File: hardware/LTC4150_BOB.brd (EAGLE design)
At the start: 15.2 x 30.5 mm, 23 parts, among them U1 LTC4150

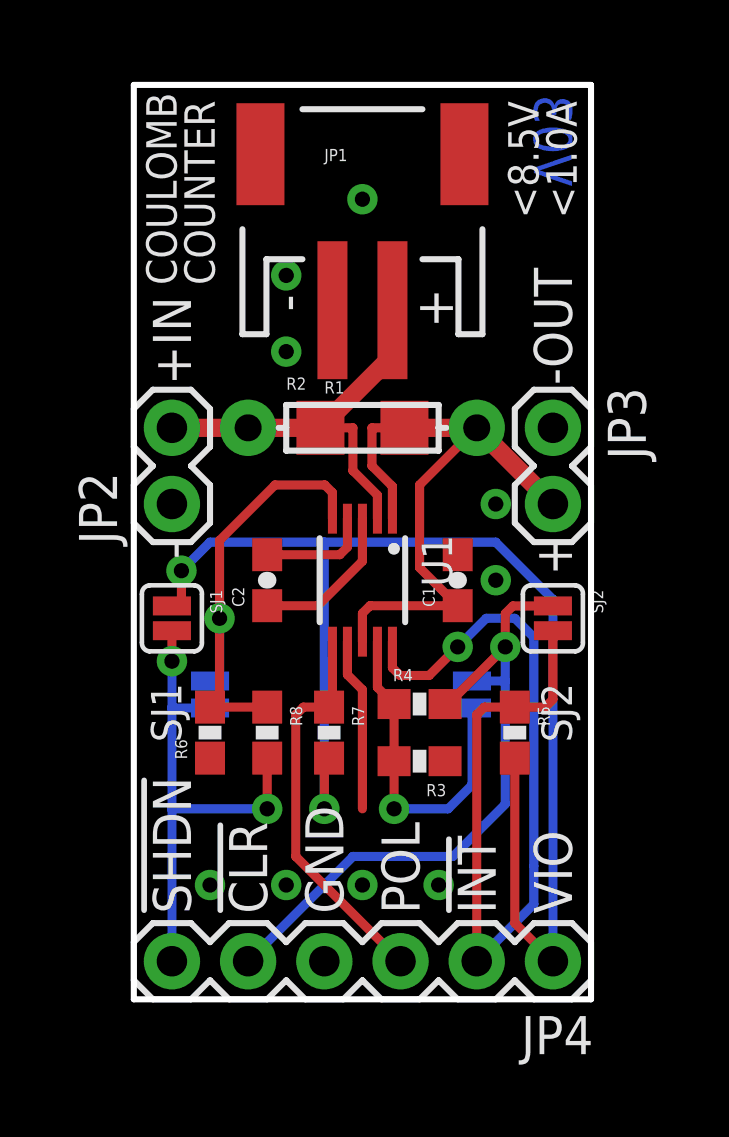
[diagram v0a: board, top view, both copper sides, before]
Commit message: Rename and rearrange repository
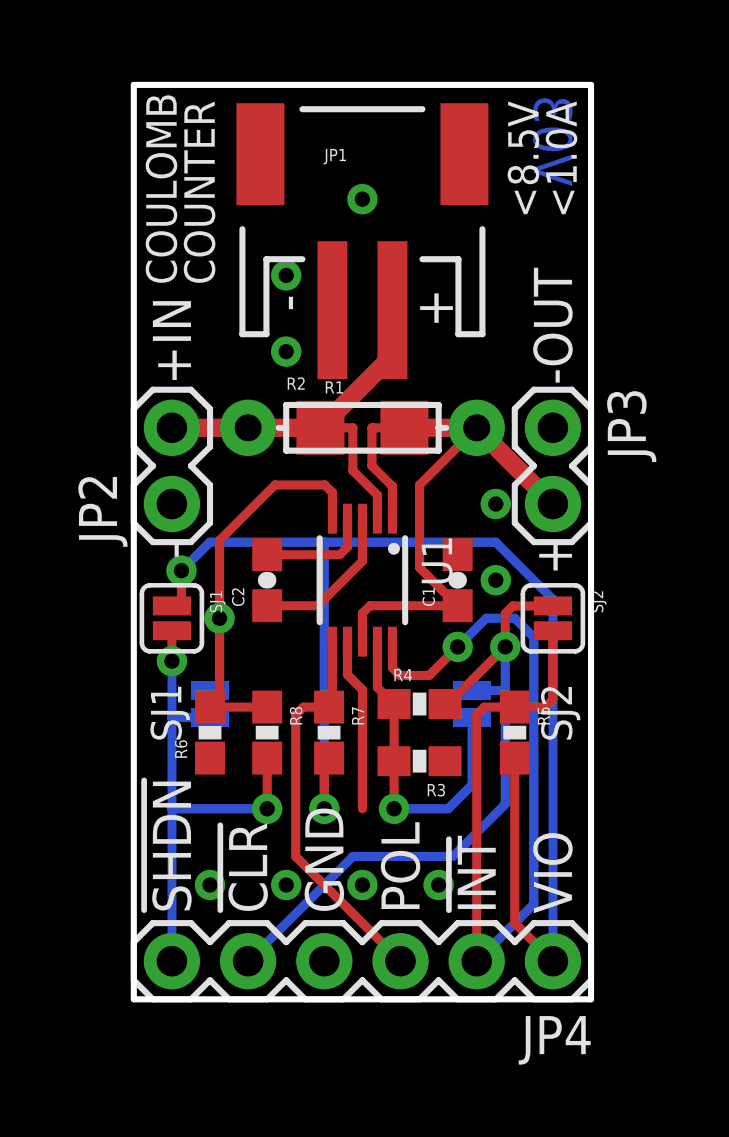
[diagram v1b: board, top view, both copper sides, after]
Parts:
- moved LOGO2 0.32 mm to (7.94, 14.0)
- moved SJ3 0.32 mm to (11.3, 9.84)
- moved SJ4 0.32 mm to (2.54, 9.84)
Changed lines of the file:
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@@
 <setting verticaltext="up"/>
 </settings>
-<grid distance="0.05" unitdist="inch" unit="inch" style="lines" multiple="2" display="yes" altdistance="0.00625" altunitdist="inch" altunit="inch"/>
+<grid distance="0.05" unitdist="inch" unit="inch" style="lines" multiple="2" display="yes" altdistance="0.0125" altunitdist="inch" altunit="inch"/>
 <layers>
-<layer number="1" name="Top" color="4" fill="1" visible="yes" active="yes"/>
+<layer number="1" name="Top" color="4" fill="1" visible="no" active="yes"/>
 <layer number="2" name="Route2" color="1" fill="3" visible="no" active="no"/>
 <layer number="3" name="Route3" color="4" fill="3" visible="no" active="no"/>
@@
 <layer number="14" name="Route14" color="1" fill="6" visible="no" active="no"/>
 <layer number="15" name="Route15" color="4" fill="6" visible="no" active="no"/>
-<layer number="16" name="Bottom" color="1" fill="1" visible="no" active="yes"/>
+<layer number="16" name="Bottom" color="1" fill="1" visible="yes" active="yes"/>
 <layer number="17" name="Pads" color="2" fill="1" visible="yes" active="yes"/>
 <layer number="18" name="Vias" color="2" fill="1" visible="yes" active="yes"/>
 <layer number="19" name="Unrouted" color="6" fill="1" visible="yes" active="yes"/>
 <layer number="20" name="Dimension" color="15" fill="1" visible="yes" active="yes"/>
-<layer number="21" name="tPlace" color="7" fill="1" visible="yes" active="yes"/>
-<layer number="22" name="bPlace" color="7" fill="1" visible="no" active="yes"/>
-<layer number="23" name="tOrigins" color="15" fill="1" visible="yes" active="yes"/>
-<layer number="24" name="bOrigins" color="15" fill="1" visible="no" active="yes"/>
+<layer number="21" name="tPlace" color="7" fill="1" visible="no" active="yes"/>
+<layer number="22" name="bPlace" color="7" fill="1" visible="yes" active="yes"/>
+<layer number="23" name="tOrigins" color="15" fill="1" visible="no" active="yes"/>
+<layer number="24" name="bOrigins" color="15" fill="1" visible="yes" active="yes"/>
 <layer number="25" name="tNames" color="7" fill="1" visible="no" active="yes"/>
 <layer number="26" name="bNames" color="7" fill="1" visible="no" active="yes"/>
 <layer number="27" name="tValues" color="7" fill="1" visible="no" active="yes"/>
 <layer number="28" name="bValues" color="7" fill="1" visible="no" active="yes"/>
-<layer number="29" name="tStop" color="7" fill="3" visible="yes" active="yes"/>
-<layer number="30" name="bStop" color="7" fill="6" visible="no" active="yes"/>
-<layer number="31" name="tCream" color="7" fill="4" visible="yes" active="yes"/>
-<layer number="32" name="bCream" color="7" fill="5" visible="no" active="yes"/>
+<layer number="29" name="tStop" color="7" fill="3" visible="no" active="yes"/>
+<layer number="30" name="bStop" color="7" fill="6" visible="yes" active="yes"/>
+<layer number="31" name="tCream" color="7" fill="4" visible="no" active="yes"/>
+<layer number="32" name="bCream" color="7" fill="5" visible="yes" active="yes"/>
 <layer number="33" name="tFinish" color="6" fill="3" visible="no" active="yes"/>
 <layer number="34" name="bFinish" color="6" fill="6" visible="no" active="yes"/>
@@
 <layer number="38" name="bTest" color="7" fill="1" visible="no" active="yes"/>
 <layer number="39" name="tKeepout" color="4" fill="11" visible="no" active="yes"/>
-<layer number="40" name="bKeepout" color="1" fill="11" visible="no" active="yes"/>
+<layer number="40" name="bKeepout" color="1" fill="11" visible="yes" active="yes"/>
 <layer number="41" name="tRestrict" color="4" fill="10" visible="no" active="yes"/>
 <layer number="42" name="bRestrict" color="1" fill="10" visible="no" active="yes"/>
@@
 <layer number="49" name="Reference" color="7" fill="1" visible="no" active="yes"/>
 <layer number="50" name="dxf" color="7" fill="1" visible="no" active="no"/>
-<layer number="51" name="tDocu" color="7" fill="1" visible="yes" active="yes"/>
-<layer number="52" name="bDocu" color="7" fill="1" visible="no" active="yes"/>
+<layer number="51" name="tDocu" color="7" fill="1" visible="no" active="yes"/>
+<layer number="52" name="bDocu" color="7" fill="1" visible="yes" active="yes"/>
 <layer number="53" name="tGND_GNDA" color="7" fill="9" visible="no" active="no"/>
 <layer number="54" name="bGND_GNDA" color="1" fill="9" visible="no" active="no"/>
@@
 <text x="13.335" y="2.8575" size="1.27" layer="22" ratio="15" rot="SMR90">VIO</text>
 <text x="8.255" y="25.0825" size="1.27" layer="22" ratio="15" rot="MR270">LTC4150</text>
-<text x="6.35" y="29.21" size="1.27" layer="22" ratio="15" rot="MR270">Coulomb Counter</text>
+<text x="6.6675" y="29.21" size="1.27" layer="22" ratio="15" rot="MR270">Coulomb Counter</text>
 <text x="14.605" y="30.1625" size="1.27" layer="16" ratio="20" rot="MR270">V03</text>
 <text x="0.635" y="20.6375" size="1.27" layer="22" ratio="15" rot="SMR90">+IN</text>
 <text x="13.335" y="20.6375" size="1.27" layer="22" ratio="15" rot="MR90">-OUT</text>
-<text x="12.54125" y="8.89" size="1.016" layer="22" ratio="15" rot="MR90">SJ3</text>
+<text x="12.54125" y="8.5725" size="1.016" layer="22" ratio="15" rot="MR90">SJ3</text>
 <text x="14.605" y="8.5725" size="1.016" layer="21" ratio="15" rot="R90">SJ2</text>
 <wire x1="0" y1="0" x2="15.24" y2="0" width="0.2032" layer="20"/>
@@
 <text x="1.42875" y="23.8125" size="1.016" layer="21" font="vector" ratio="15" rot="R90">COULOMB</text>
 <text x="2.69875" y="23.8125" size="1.016" layer="21" font="vector" ratio="15" rot="R90">COUNTER</text>
-<text x="3.81" y="8.89" size="1.016" layer="22" ratio="15" rot="MR90">SJ4</text>
+<text x="3.81" y="8.5725" size="1.016" layer="22" ratio="15" rot="MR90">SJ4</text>
 <text x="10.63625" y="22.38375" size="1.27" layer="21" font="vector" ratio="15" rot="R90">+</text>
 <text x="4.445" y="23.495" size="1.27" layer="21" font="vector" ratio="15" rot="R270">-</text>
@@
 <element name="LOGO3" library="SparkFun-Aesthetics" package="SFE-LOGO-FLAME" value="LOGO-SFESK" x="8.89" y="26.67" rot="MR90"/>
 <element name="LOGO1" library="SparkFun-Aesthetics" package="OSHW-LOGO-S" value="OSHW-LOGOS" x="1.905" y="28.2575" rot="MR90"/>
-<element name="SJ3" library="SparkFun-Passives" package="SJ_2S-NO" value="" x="11.27125" y="10.16" rot="MR90"/>
+<element name="SJ3" library="SparkFun-Passives" package="SJ_2S-NO" value="" x="11.27125" y="9.8425" rot="MR90"/>
 <element name="SJ1" library="SparkFun-Passives" package="SJ_2S" value="" x="1.27" y="12.7" rot="R270"/>
-<element name="LOGO2" library="SparkFun-Aesthetics" package="SFE-NEW-WEB" value="LOGO-SFENW2" x="8.255" y="13.97" rot="MR90"/>
+<element name="LOGO2" library="SparkFun-Aesthetics" package="SFE-NEW-WEB" value="LOGO-SFENW2" x="7.9375" y="13.97" rot="MR90"/>
 <element name="SJ2" library="SparkFun-Passives" package="SJ_2S" value="" x="13.97" y="12.7" rot="R270"/>
 <element name="R2" library="SparkFun-Passives" package="AXIAL-0.3" value="DNP" x="7.62" y="19.05" smashed="yes">
 <attribute name="NAME" x="5.08" y="20.32" size="0.4064" layer="25" font="vector"/>
 </element>
-<element name="SJ4" library="SparkFun-Passives" package="SJ_2S-NO" value="" x="2.54" y="10.16" rot="MR270"/>
+<element name="SJ4" library="SparkFun-Passives" package="SJ_2S-NO" value="" x="2.54" y="9.8425" rot="MR270"/>
 </elements>
 <signals>
@@
 <contactref element="SJ4" pad="1"/>
 <via x="2.8575" y="12.7" extent="1-16" drill="0.508"/>
-<wire x1="2.54" y1="10.61" x2="2.8575" y2="10.61" width="0.3048" layer="16"/>
-<wire x1="2.8575" y1="10.61" x2="2.8575" y2="12.7" width="0.3048" layer="16"/>
+<wire x1="2.54" y1="10.2925" x2="2.8575" y2="10.2925" width="0.3048" layer="16"/>
+<wire x1="2.8575" y1="10.2925" x2="2.8575" y2="12.7" width="0.3048" layer="16"/>
 </signal>
 <signal name="!SHDN!">
@@
 <contactref element="SJ4" pad="2"/>
 <contactref element="JP4" pad="6"/>
-<wire x1="1.27" y1="9.71" x2="1.27" y2="6.35" width="0.3048" layer="16"/>
+<wire x1="1.27" y1="9.3925" x2="1.27" y2="6.35" width="0.3048" layer="16"/>
 <wire x1="1.27" y1="6.35" x2="1.27" y2="1.27" width="0.3048" layer="16"/>
 <wire x1="4.445" y1="8.04" x2="4.445" y2="6.35" width="0.3048" layer="1"/>
 <via x="4.445" y="6.35" extent="1-16" drill="0.508"/>
 <wire x1="4.445" y1="6.35" x2="1.27" y2="6.35" width="0.3048" layer="16"/>
-<wire x1="1.27" y1="9.71" x2="2.54" y2="9.71" width="0.3048" layer="16"/>
-<wire x1="1.27" y1="9.71" x2="1.27" y2="11.27125" width="0.3048" layer="16"/>
+<wire x1="1.27" y1="9.3925" x2="2.54" y2="9.3925" width="0.3048" layer="16"/>
+<wire x1="1.27" y1="9.3925" x2="1.27" y2="11.27125" width="0.3048" layer="16"/>
 </signal>
 <signal name="GND">
@@
 <wire x1="12.3825" y1="11.7475" x2="10.4775" y2="9.8425" width="0.3048" layer="1"/>
 <wire x1="10.4775" y1="9.8425" x2="10.375" y2="9.8425" width="0.3048" layer="1"/>
-<wire x1="11.27125" y1="10.61" x2="12.3825" y2="10.61" width="0.3048" layer="16"/>
-<wire x1="12.3825" y1="10.61" x2="12.3825" y2="11.7475" width="0.3048" layer="16"/>
+<wire x1="11.27125" y1="10.2925" x2="12.3825" y2="10.2925" width="0.3048" layer="16"/>
+<wire x1="12.3825" y1="10.2925" x2="12.3825" y2="11.7475" width="0.3048" layer="16"/>
 <contactref element="JP4" pad="5"/>
 <wire x1="3.81" y1="1.27" x2="7.3025" y2="4.7625" width="0.3048" layer="16"/>
 <wire x1="7.3025" y1="4.7625" x2="10.63625" y2="4.7625" width="0.3048" layer="16"/>
 <wire x1="10.63625" y1="4.7625" x2="12.3825" y2="6.50875" width="0.3048" layer="16"/>
-<wire x1="12.3825" y1="6.50875" x2="12.3825" y2="10.61" width="0.3048" layer="16"/>
+<wire x1="12.3825" y1="6.50875" x2="12.3825" y2="10.2925" width="0.3048" layer="16"/>
 </signal>
 <signal name="N$1">
@@
 <via x="8.675" y="6.35" extent="1-16" drill="0.508"/>
 <wire x1="8.675" y1="6.35" x2="10.4775" y2="6.35" width="0.3048" layer="16"/>
-<wire x1="11.27125" y1="9.71" x2="11.27125" y2="7.14375" width="0.3048" layer="16"/>
+<wire x1="11.27125" y1="9.3925" x2="11.27125" y2="7.14375" width="0.3048" layer="16"/>
 <wire x1="11.27125" y1="7.14375" x2="10.4775" y2="6.35" width="0.3048" layer="16"/>
 </signal>

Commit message: Changed version to 1.0 for reds
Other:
- board text added: "V10"
- board text removed: "V03"
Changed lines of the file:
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@@
 <grid distance="0.05" unitdist="inch" unit="inch" style="lines" multiple="2" display="yes" altdistance="0.0125" altunitdist="inch" altunit="inch"/>
 <layers>
-<layer number="1" name="Top" color="4" fill="1" visible="no" active="yes"/>
+<layer number="1" name="Top" color="4" fill="1" visible="yes" active="yes"/>
 <layer number="2" name="Route2" color="1" fill="3" visible="no" active="no"/>
 <layer number="3" name="Route3" color="4" fill="3" visible="no" active="no"/>
@@
 <layer number="19" name="Unrouted" color="6" fill="1" visible="yes" active="yes"/>
 <layer number="20" name="Dimension" color="15" fill="1" visible="yes" active="yes"/>
-<layer number="21" name="tPlace" color="7" fill="1" visible="no" active="yes"/>
-<layer number="22" name="bPlace" color="7" fill="1" visible="yes" active="yes"/>
-<layer number="23" name="tOrigins" color="15" fill="1" visible="no" active="yes"/>
-<layer number="24" name="bOrigins" color="15" fill="1" visible="yes" active="yes"/>
+<layer number="21" name="tPlace" color="7" fill="1" visible="yes" active="yes"/>
+<layer number="22" name="bPlace" color="7" fill="1" visible="no" active="yes"/>
+<layer number="23" name="tOrigins" color="15" fill="1" visible="yes" active="yes"/>
+<layer number="24" name="bOrigins" color="15" fill="1" visible="no" active="yes"/>
 <layer number="25" name="tNames" color="7" fill="1" visible="no" active="yes"/>
 <layer number="26" name="bNames" color="7" fill="1" visible="no" active="yes"/>
 <layer number="27" name="tValues" color="7" fill="1" visible="no" active="yes"/>
 <layer number="28" name="bValues" color="7" fill="1" visible="no" active="yes"/>
-<layer number="29" name="tStop" color="7" fill="3" visible="no" active="yes"/>
-<layer number="30" name="bStop" color="7" fill="6" visible="yes" active="yes"/>
-<layer number="31" name="tCream" color="7" fill="4" visible="no" active="yes"/>
-<layer number="32" name="bCream" color="7" fill="5" visible="yes" active="yes"/>
+<layer number="29" name="tStop" color="7" fill="3" visible="yes" active="yes"/>
+<layer number="30" name="bStop" color="7" fill="6" visible="no" active="yes"/>
+<layer number="31" name="tCream" color="7" fill="4" visible="yes" active="yes"/>
+<layer number="32" name="bCream" color="7" fill="5" visible="no" active="yes"/>
 <layer number="33" name="tFinish" color="6" fill="3" visible="no" active="yes"/>
 <layer number="34" name="bFinish" color="6" fill="6" visible="no" active="yes"/>
@@
 <layer number="37" name="tTest" color="7" fill="1" visible="no" active="yes"/>
 <layer number="38" name="bTest" color="7" fill="1" visible="no" active="yes"/>
-<layer number="39" name="tKeepout" color="4" fill="11" visible="no" active="yes"/>
-<layer number="40" name="bKeepout" color="1" fill="11" visible="yes" active="yes"/>
+<layer number="39" name="tKeepout" color="4" fill="11" visible="yes" active="yes"/>
+<layer number="40" name="bKeepout" color="1" fill="11" visible="no" active="yes"/>
 <layer number="41" name="tRestrict" color="4" fill="10" visible="no" active="yes"/>
 <layer number="42" name="bRestrict" color="1" fill="10" visible="no" active="yes"/>
@@
 <layer number="49" name="Reference" color="7" fill="1" visible="no" active="yes"/>
 <layer number="50" name="dxf" color="7" fill="1" visible="no" active="no"/>
-<layer number="51" name="tDocu" color="7" fill="1" visible="no" active="yes"/>
-<layer number="52" name="bDocu" color="7" fill="1" visible="yes" active="yes"/>
+<layer number="51" name="tDocu" color="7" fill="1" visible="yes" active="yes"/>
+<layer number="52" name="bDocu" color="7" fill="1" visible="no" active="yes"/>
 <layer number="53" name="tGND_GNDA" color="7" fill="9" visible="no" active="no"/>
 <layer number="54" name="bGND_GNDA" color="1" fill="9" visible="no" active="no"/>
@@
 <text x="8.255" y="25.0825" size="1.27" layer="22" ratio="15" rot="MR270">LTC4150</text>
 <text x="6.6675" y="29.21" size="1.27" layer="22" ratio="15" rot="MR270">Coulomb Counter</text>
-<text x="14.605" y="30.1625" size="1.27" layer="16" ratio="20" rot="MR270">V03</text>
+<text x="14.605" y="30.1625" size="1.27" layer="16" ratio="20" rot="MR270">V10</text>
 <text x="0.635" y="20.6375" size="1.27" layer="22" ratio="15" rot="SMR90">+IN</text>
 <text x="13.335" y="20.6375" size="1.27" layer="22" ratio="15" rot="MR90">-OUT</text>

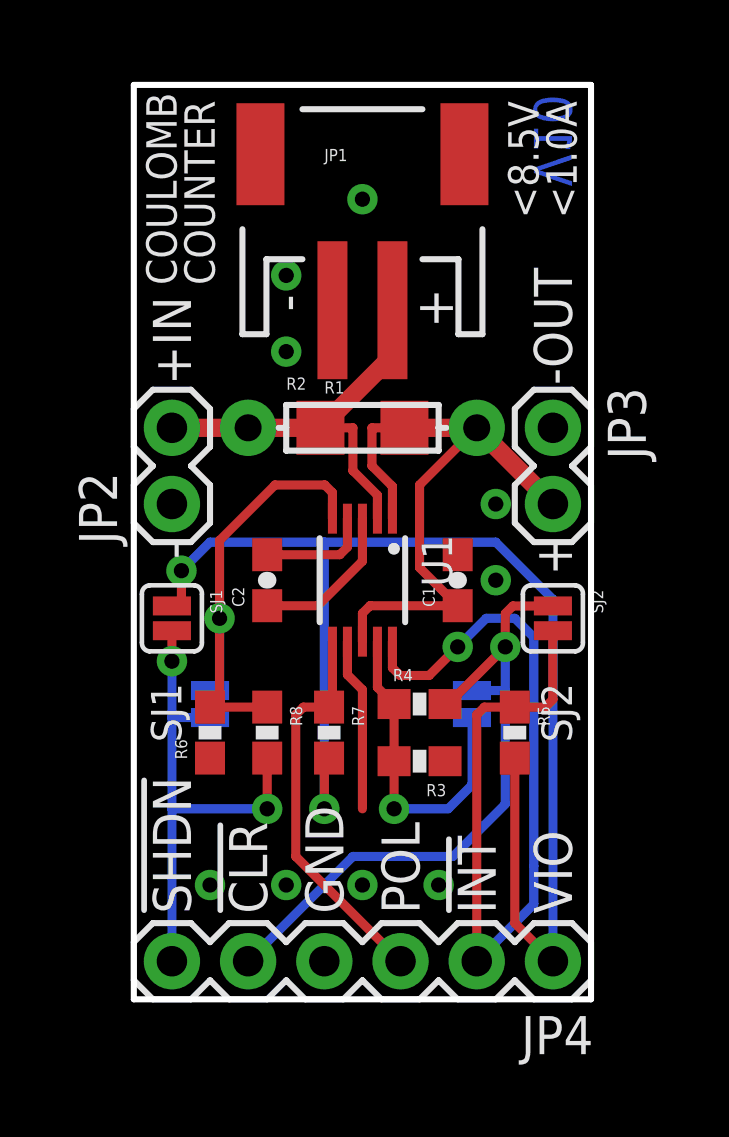
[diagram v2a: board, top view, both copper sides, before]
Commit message: Replaced solder jumper with pullup resistor
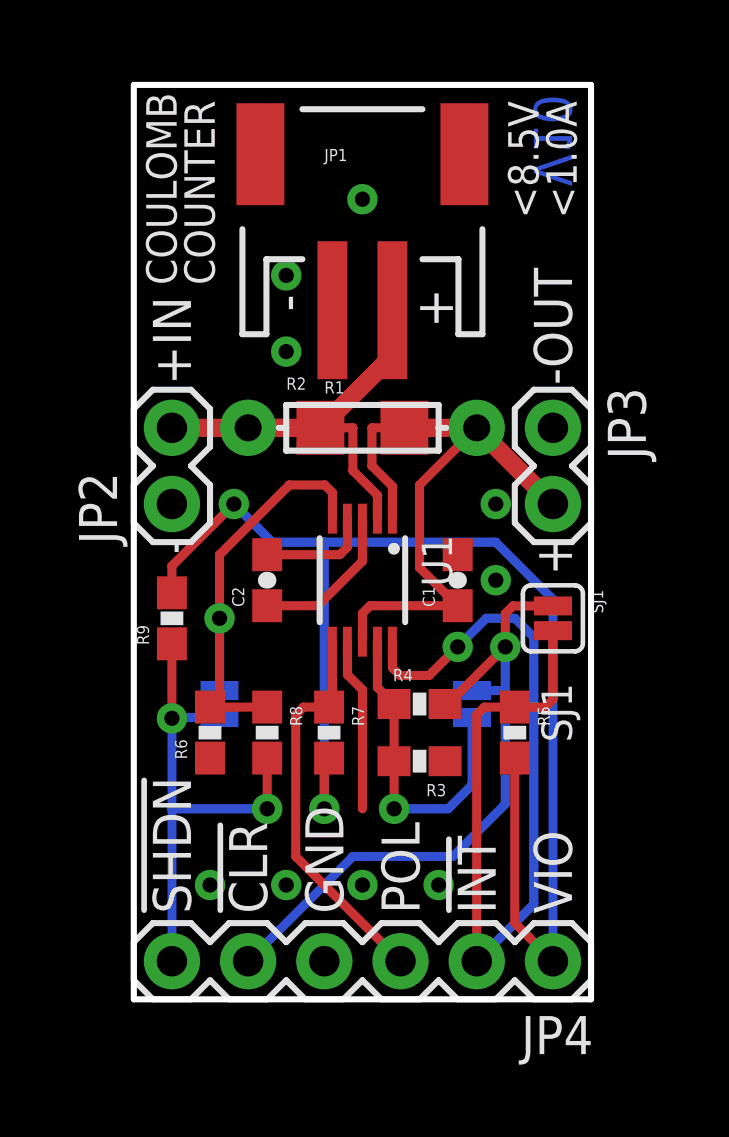
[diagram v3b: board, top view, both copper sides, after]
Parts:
- removed SJ4: (no value), SparkFun-Passives:SJ_2S-NO
- added R9: 3.3K, SparkFun-Passives:0603-RES
- SJ2: device SparkFun-Passives:SJ_2S -> SparkFun-Passives:SJ_2S-NO
- moved SJ1 12.7 mm to (14.0, 12.7)
- moved SJ3 8.41 mm to (2.86, 9.84), turned to 270 degrees
- moved SJ2 3.93 mm to (11.3, 9.84), flipped to the bottom, turned to 90 degrees
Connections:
- net !CLR!: now also SJ1.1, SJ2.2; no longer SJ2.1, SJ3.2
- net !INT!: now also SJ1.2; no longer SJ2.2
- net !SHDN!: now also R9.1, SJ3.2; no longer SJ1.2, SJ4.2
- net N$1: now also SJ2.1; no longer SJ3.1
- net N$9: now also SJ3.1; no longer SJ4.1
- net VIO: now also R9.2; no longer SJ1.1
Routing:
- net VIO: track 45.2 -> 45.9 mm
- net N$9: track 15.7 -> 15.1 mm
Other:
- board text removed: "SJ4"
